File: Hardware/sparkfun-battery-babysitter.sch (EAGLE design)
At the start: 58 parts, among them U1 BQ24075, U2 BQ27441-G1

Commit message: Removing temp library, and updating libs in eagle files.
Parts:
- U1: device battery-management-temp:BQ24075 -> SparkFun-PowerIC:BQ24075
- U2: device battery-management-temp:BQ27441-G1 -> SparkFun-PowerIC:BQ27441-G1
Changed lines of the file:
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@@
 <part name="GND3" library="SparkFun-Aesthetics" deviceset="GND" device=""/>
 <part name="SUPPLY1" library="SparkFun-Aesthetics" deviceset="V_USB" device=""/>
-<part name="U2" library="battery-management-temp" deviceset="BQ27441-G1" device="">
+<part name="U2" library="SparkFun-PowerIC" deviceset="BQ27441-G1" device="">
 <attribute name="PROD_ID" value="IC-13220"/>
 </part>
@@
 <part name="R13" library="SparkFun-Resistors" deviceset="4.7KOHM-1/10W-1%(0603)" device="" value="4.7K"/>
 <part name="R14" library="SparkFun-Resistors" deviceset="4.7KOHM-1/10W-1%(0603)" device="" value="4.7K"/>
-<part name="U1" library="battery-management-temp" deviceset="BQ24075" device="">
+<part name="U1" library="SparkFun-PowerIC" deviceset="BQ24075" device="">
 <attribute name="PROD_ID" value="IC-13219"/>
 </part>

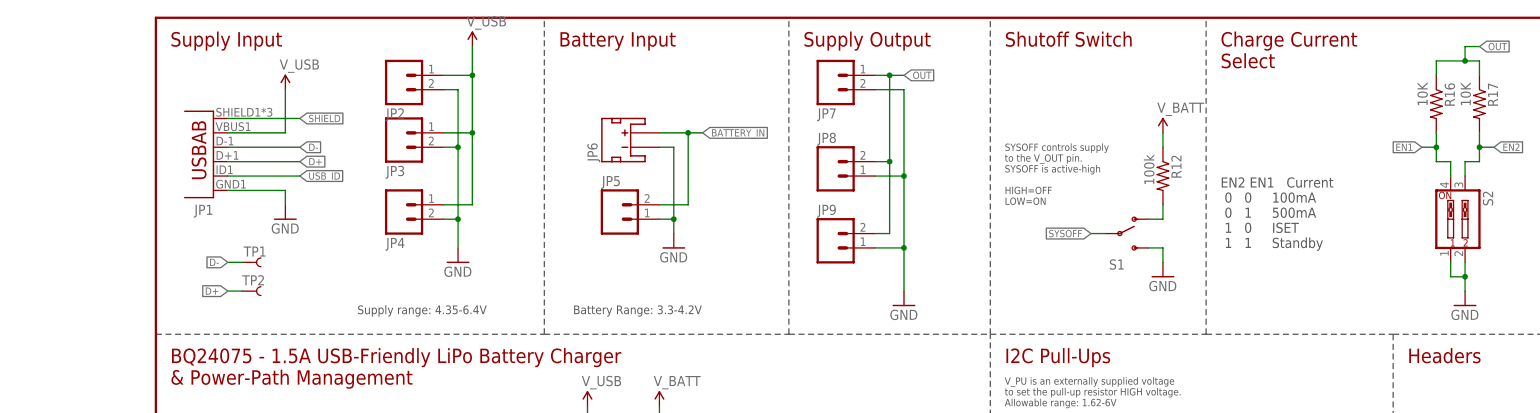
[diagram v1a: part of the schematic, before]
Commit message: Values Added to 3 Part on .brd/.sch
USB-AB-MICRO-SMD_V03
SW_DIP-2_SMD
RIGHT_ANGLE_SLIDE_SWITCH_SMD
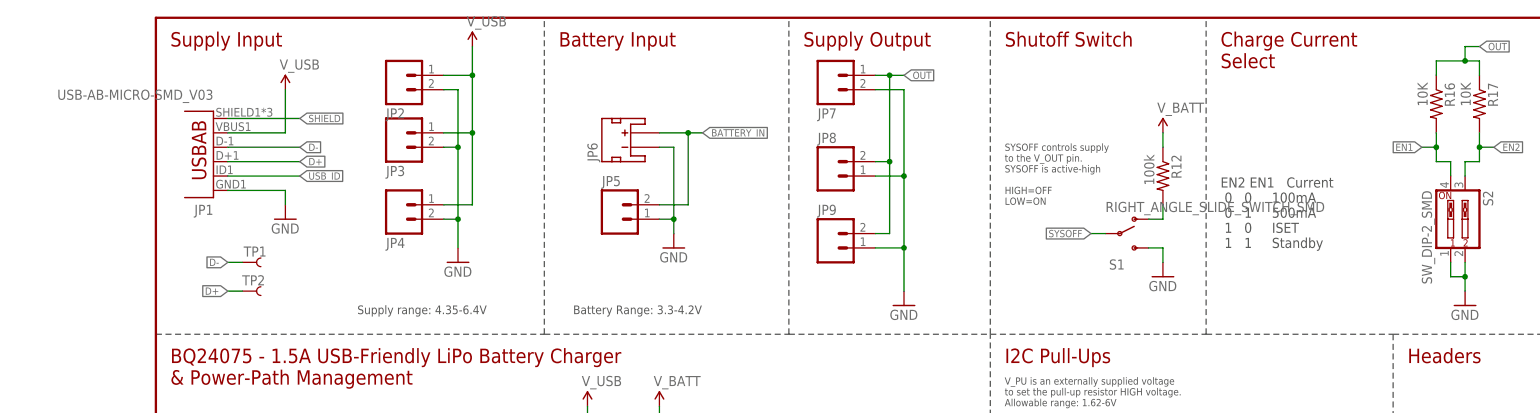
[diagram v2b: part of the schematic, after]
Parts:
- JP1: value (none) -> USB-AB-MICRO-SMD_V03
- S1: value (none) -> RIGHT_ANGLE_SLIDE_SWITCH_SMD
- S2: value (none) -> SW_DIP-2_SMD
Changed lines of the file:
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@@
 <?xml version="1.0" encoding="utf-8"?>
 <!DOCTYPE eagle SYSTEM "eagle.dtd">
-<eagle version="7.5.0">
+<eagle version="7.7.0">
 <drawing>
 <settings>
@@
 <parts>
 <part name="FRAME1" library="SparkFun-Aesthetics" deviceset="FRAME-LETTER" device=""/>
-<part name="JP1" library="SparkFun-Connectors" deviceset="USB-AB" device="CONN-11794"/>
+<part name="JP1" library="SparkFun-Connectors" deviceset="USB-AB" device="CONN-11794" value="USB-AB-MICRO-SMD_V03"/>
 <part name="JP6" library="SparkFun-Connectors" deviceset="JST_2MM_MALE" device=""/>
 <part name="GND13" library="SparkFun-Aesthetics" deviceset="GND" device=""/>
@@
 <part name="STANDOFF2" library="SparkFun-Electromechanical" deviceset="STAND-OFF" device=""/>
 <part name="STANDOFF4" library="SparkFun-Electromechanical" deviceset="STAND-OFF" device=""/>
-<part name="S1" library="SparkFun-Electromechanical" deviceset="SWITCH-SPDT" device="-SMD-A"/>
+<part name="S1" library="SparkFun-Electromechanical" deviceset="SWITCH-SPDT" device="-SMD-A" value="RIGHT_ANGLE_SLIDE_SWITCH_SMD"/>
 <part name="JP3" library="SparkFun-Connectors" deviceset="M02" device="3.5MM-NO_SILK"/>
 <part name="JP7" library="SparkFun-Connectors" deviceset="M02" device="3.5MM-NO_SILK"/>
@@
 <part name="FID1" library="SparkFun-Aesthetics" deviceset="FIDUCIAL" device="1X2"/>
 <part name="FID2" library="SparkFun-Aesthetics" deviceset="FIDUCIAL" device="1X2"/>
-<part name="S2" library="SparkFun-Electromechanical" deviceset="SW_DIP-2" device="-SMT-HALFSIZE">
+<part name="S2" library="SparkFun-Electromechanical" deviceset="SW_DIP-2" device="-SMT-HALFSIZE" value="SW_DIP-2_SMD">
 <attribute name="PROD_ID" value="SWCH-13215"/>
 </part>
